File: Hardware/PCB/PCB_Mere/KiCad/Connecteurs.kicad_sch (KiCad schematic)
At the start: 9 parts, among them CN5 B2B-PH-K-S_FILLE_ALIM, CN6 B2B-PH-K-S_GNSS_ALIM, U5 B8B-PH-K-S-, U6 B8B-PH-K-S_FILS

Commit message: push du kicad
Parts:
- removed C30: 100n, symbol Device:C_Small
- removed CN5: B2B-PH-K-S_FILLE_ALIM, EasyEDA:CONN-TH_B2B-PH-K-S, symbol EasyEDA:B2B-PH-K-S
- removed CN6: B2B-PH-K-S_GNSS_ALIM, EasyEDA:CONN-TH_B2B-PH-K-S, symbol EasyEDA:B2B-PH-K-S
- removed H2: PZ254-1-20-Z-8.5, EasyEDA:HDR-TH_20P-P2.54-V-M, symbol EasyEDA:PZ254-1-20-Z-8.5
- added C36, C37, C38: 100n, symbol Device:C_Small
- added CN2: B4B-PH-K-S_GNSS, EasyEDA:CONN-TH_B4B-PH-K-S, symbol EasyEDA:B4B-PH-K-S
- added H3: PZ254-1-10-Z-8.5_EL, EasyEDA:HDR-TH_10P-P2.54-V-M, symbol EasyEDA:PZ254-1-10-Z-8.5
- added U7: B10B-PH-K-S-_SCRN/JOY/ALIM, EasyEDA:CONN-TH_B10B-PH-K-S-LF-SN, symbol EasyEDA:B10B-PH-K-S-
- H1: value PZ254-1-20-Z-8.5 -> PZ254-1-20-Z-8.5_AZ
- U5: value B8B-PH-K-S- -> B8B-PH-K-S-_TACTIL
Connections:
- net +3.3V: now also C37.2, U7.2
- net +5V: now also H1.1, H1.2, C36.1, C36.2, C37.1, C38.1, C38.2, CN2.1, CN2.2, U7.1; no longer U5.1
- net LIDAR_UART8_RX: now also U6.8; no longer U6.7
- net LIDAR_UART8_TX: now also U6.7; no longer U6.8
- net STEPPER-EL_TIM1_CH1: now also H3.10
- net TMC2209_EL_DIAG_GPIO_Input: now also H3.4
- net TMC2209_EL_DIR_GPIO_Output: now also H3.7
- net TMC2209_EL_ENABLE_GPIO_Output: now also H3.9
- net TMC2209_EL_INDEX_GPIO_Input: now also H3.3
- net TMC2209_EL_MS1_GPIO_Output: now also H3.6
- net TMC2209_EL_MS2_GPIO_Output: now also H3.5
- net TMC2209_EL_STEP_GPIO_Output: now also H3.8
- net TMC2209_EL_USART3_RX: now also H3.2
- net TMC2209_EL_USART3_TX: now also H3.1
- net BONUS1_GPIO: now reaches U5.2
- net ETAT-B-ON/OFF_GPIO_Input: now reaches U5.3
- net TACTIL_GPIO_EXTI4: now reaches U5.4
- net TACTIL_SPI6_MOSI: now reaches U5.5
- net TACTIL_SPI6_MISO: now reaches U5.6
- net TACTIL_SPI6_SCK: now reaches U5.7
- net TACTIL_SPI6_NSS: now reaches U5.8
- new net BONUS2_GPIO: U5.1
- new net GNSS_UART5_RX: CN2.4
- new net GNSS_UART5_TX: CN2.3
- new net JOYSTICK_ADC1_INP10: U7.5
- new net JOYSTICK_ADC1_INP11: U7.4
- new net JOYSTICK_GPIO_Input: U7.3
- new net SCREEN_RST_GPIO_Output: U7.6
- new net SCREEN_SPI5_MISO: U7.8
- new net SCREEN_SPI5_MOSI: U7.7
- new net SCREEN_SPI5_NSS: U7.10
- new net SCREEN_SPI5_SCK: U7.9
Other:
- note removed: "Puissance"
- note removed: "Signal"

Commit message: Dernière version Schématique
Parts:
- C31, C32, C36, C37, C38: footprint (none) -> Capacitor_SMD:C_0201_0603Metric; LCSC Part (none) -> C49062
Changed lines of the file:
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@@
 		(dnp no)
 		(property "Reference" "C32"
-			(at 243.84 47.752 90)
+			(at 242.57 30.226 90)
 			(show_name no)
 			(do_not_autoplace no)
@@
 		)
 		(property "Value" "100n"
-			(at 243.84 53.594 90)
-			(show_name no)
-			(do_not_autoplace no)
-			(effects
-				(font
-					(size 1.27 1.27)
-				)
-			)
-		)
-		(property "Footprint" ""
+			(at 241.046 33.02 90)
+			(show_name no)
+			(do_not_autoplace no)
+			(effects
+				(font
+					(size 1.27 1.27)
+				)
+			)
+		)
+		(property "Footprint" "Capacitor_SMD:C_0201_0603Metric"
 			(at 243.84 33.02 0)
 			(hide yes)
@@
 		(property "Description" "Unpolarized capacitor, small symbol"
 			(at 243.84 33.02 0)
+			(hide yes)
+			(show_name no)
+			(do_not_autoplace no)
+			(effects
+				(font
+					(size 1.27 1.27)
+				)
+			)
+		)
+		(property "LCSC Part" "C49062"
+			(at 243.84 33.02 90)
 			(hide yes)
 			(show_name no)
@@
 		(dnp no)
 		(property "Reference" "C31"
-			(at 243.84 38.862 90)
+			(at 246.634 24.13 90)
 			(show_name no)
 			(do_not_autoplace no)
@@
 		)
 		(property "Value" "100n"
-			(at 243.84 44.704 90)
-			(show_name no)
-			(do_not_autoplace no)
-			(effects
-				(font
-					(size 1.27 1.27)
-				)
-			)
-		)
-		(property "Footprint" ""
+			(at 241.046 24.638 90)
+			(show_name no)
+			(do_not_autoplace no)
+			(effects
+				(font
+					(size 1.27 1.27)
+				)
+			)
+		)
+		(property "Footprint" "Capacitor_SMD:C_0201_0603Metric"
 			(at 243.84 24.13 0)
 			(hide yes)
@@
 		(property "Description" "Unpolarized capacitor, small symbol"
 			(at 243.84 24.13 0)
+			(hide yes)
+			(show_name no)
+			(do_not_autoplace no)
+			(effects
+				(font
+					(size 1.27 1.27)
+				)
+			)
+		)
+		(property "LCSC Part" "C49062"
+			(at 243.84 24.13 90)
 			(hide yes)
 			(show_name no)
@@
 			)
 		)
-		(property "Footprint" ""
+		(property "Footprint" "Capacitor_SMD:C_0201_0603Metric"
 			(at 48.26 88.9 0)
 			(hide yes)
@@
 		)
 		(property "Description" "Unpolarized capacitor, small symbol"
+			(at 48.26 88.9 0)
+			(hide yes)
+			(show_name no)
+			(do_not_autoplace no)
+			(effects
+				(font
+					(size 1.27 1.27)
+				)
+			)
+		)
+		(property "LCSC Part" "C49062"
 			(at 48.26 88.9 0)
 			(hide yes)
@@
 			)
 		)
-		(property "Footprint" ""
+		(property "Footprint" "Capacitor_SMD:C_0201_0603Metric"
 			(at 168.91 105.41 0)
 			(hide yes)
@@
 		)
 		(property "Description" "Unpolarized capacitor, small symbol"
+			(at 168.91 105.41 0)
+			(hide yes)
+			(show_name no)
+			(do_not_autoplace no)
+			(effects
+				(font
+					(size 1.27 1.27)
+				)
+			)
+		)
+		(property "LCSC Part" "C49062"
 			(at 168.91 105.41 0)
 			(hide yes)
@@
 			)
 		)
-		(property "Footprint" ""
+		(property "Footprint" "Capacitor_SMD:C_0201_0603Metric"
 			(at 38.1 153.67 0)
 			(hide yes)
@@
 			(at 38.1 153.67 0)
 			(hide yes)
+			(show_name no)
+			(do_not_autoplace no)
+			(effects
+				(font
+					(size 1.27 1.27)
+				)
+			)
+		)
+		(property "LCSC Part" "C49062"
+			(at 38.1 153.67 0)
+			(hide yes)

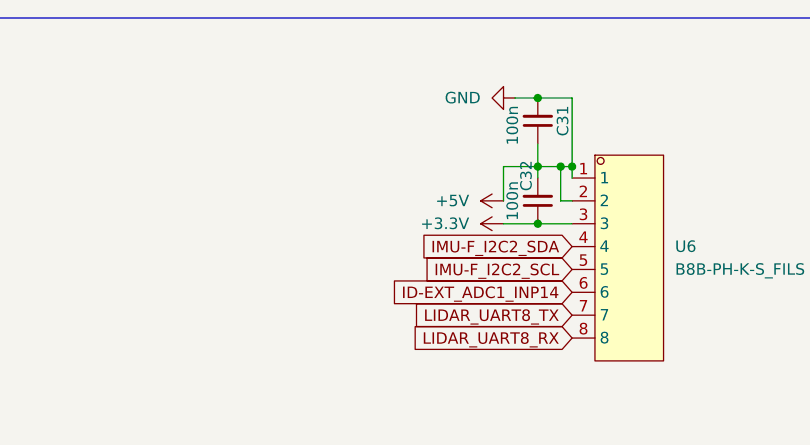
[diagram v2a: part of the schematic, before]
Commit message: Nouvelles empreintes de mounting holes et plusieurs court circuits retirés du schematic
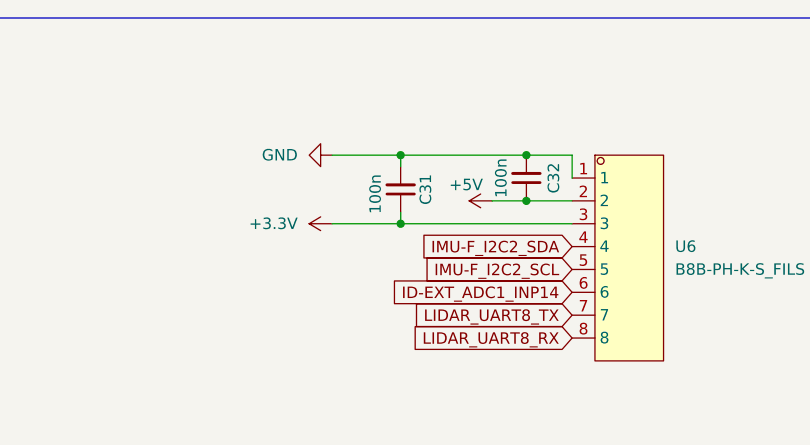
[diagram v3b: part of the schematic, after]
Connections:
- net +3.3V: now also C31.1; no longer C32.1
- net +5V: now also C32.1; no longer C31.1, C31.2, C32.2, C36.1, C37.1, C38.1, CN2.1, H1.1, U6.1, U7.1
- new net GND: C31.2, C32.2, C36.1, C37.1, C38.1, CN2.1, H1.1, U6.1, U7.1
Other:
- moved on the sheet: C31, C32

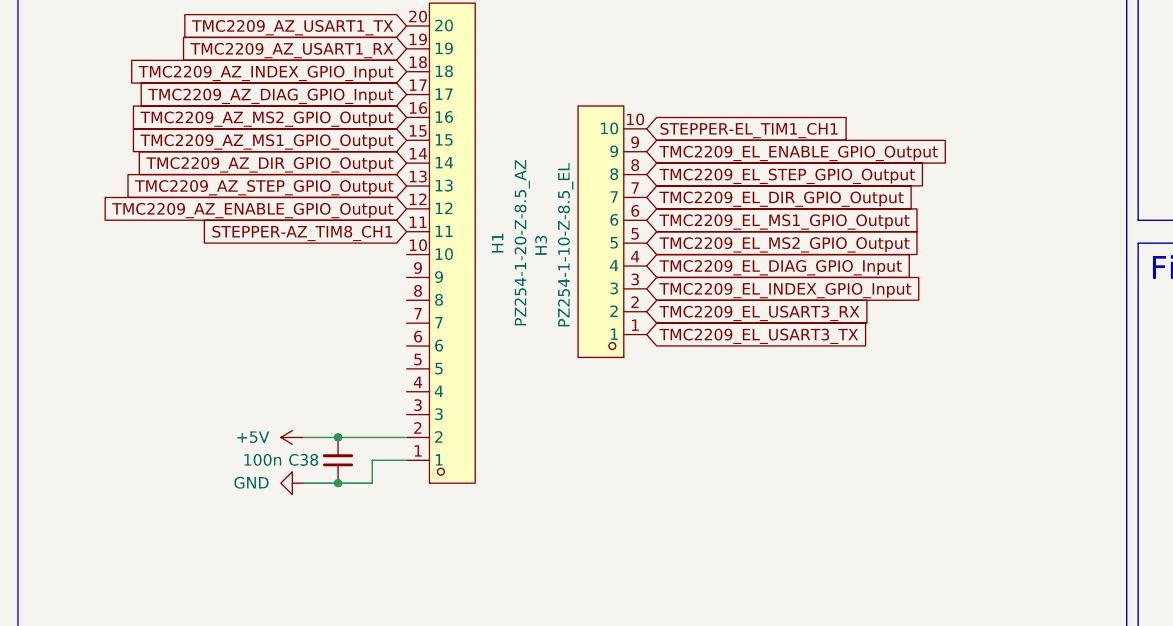
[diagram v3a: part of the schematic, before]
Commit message: Push PCB_Mère avancement routage
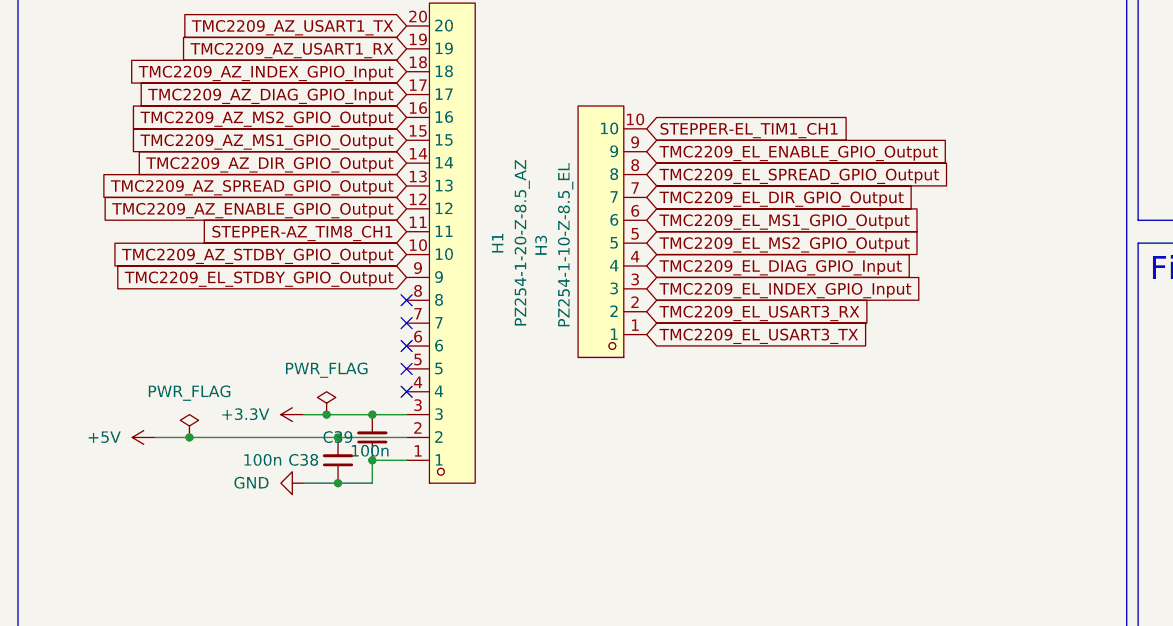
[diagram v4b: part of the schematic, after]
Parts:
- added C39: 100n, Capacitor_SMD:C_0402_1005Metric, symbol Device:C_Small
- C31, C32, C36, C37, C38: footprint Capacitor_SMD:C_0201_0603Metric -> Capacitor_SMD:C_0402_1005Metric
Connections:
- net +3.3V: now also H1.3, C39.2
- net GND: now also C39.1
- net TMC2209_AZ_STDBY_GPIO_Output: now reaches H1.10
- net TMC2209_EL_STDBY_GPIO_Output: now reaches H1.9
- net TMC2209_AZ_STEP_GPIO_Output renamed TMC2209_AZ_SPREAD_GPIO_Output
- net TMC2209_EL_STEP_GPIO_Output renamed TMC2209_EL_SPREAD_GPIO_Output
- no-connect marks 0 -> 5

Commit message: last version
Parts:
- C31, C32, C36, C37, C38, C39: LCSC Part C49062 -> C1525
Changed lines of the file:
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@@
 			)
 		)
-		(property "LCSC Part" "C49062"
+		(property "LCSC Part" "C1525"
 			(at 242.57 30.48 90)
 			(hide yes)
@@
 			)
 		)
-		(property "LCSC Part" "C49062"
+		(property "LCSC Part" "C1525"
 			(at 52.07 86.36 0)
 			(hide yes)
@@
 			)
 		)
-		(property "LCSC Part" "C49062"
+		(property "LCSC Part" "C1525"
 			(at 228.6 31.75 90)
 			(hide yes)
@@
 			)
 		)
-		(property "LCSC Part" "C49062"
+		(property "LCSC Part" "C1525"
 			(at 48.26 88.9 0)
 			(hide yes)
@@
 			)
 		)
-		(property "LCSC Part" "C49062"
+		(property "LCSC Part" "C1525"
 			(at 168.91 105.41 0)
 			(hide yes)
@@
 			)
 		)
-		(property "LCSC Part" "C49062"
+		(property "LCSC Part" "C1525"
 			(at 38.1 153.67 0)
 			(hide yes)

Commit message: last version
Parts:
- added C42: 100n, Capacitor_SMD:C_0402_1005Metric, symbol Device:C_Small
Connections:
- net +3.3V: now also H1.4, H1.5, C42.2; no longer H1.3
- net GND: now also H1.3, H1.6, H1.7, H1.8, C42.1
- no-connect marks 5 -> 0
